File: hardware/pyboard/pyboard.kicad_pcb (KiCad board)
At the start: 2 copper layers, 65 parts, among them J1 Battery, J2 Arduino_Mega2560_Shield, J6 USB_B_Micro, J9 Micro_SD_SCHA5B0200, Q1 IRLML6402, Q2 IRLML6402, SW1 RST, SW2 USR, U1 STM32F405RGT6, U2 MCP1703A-3302_SOT89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

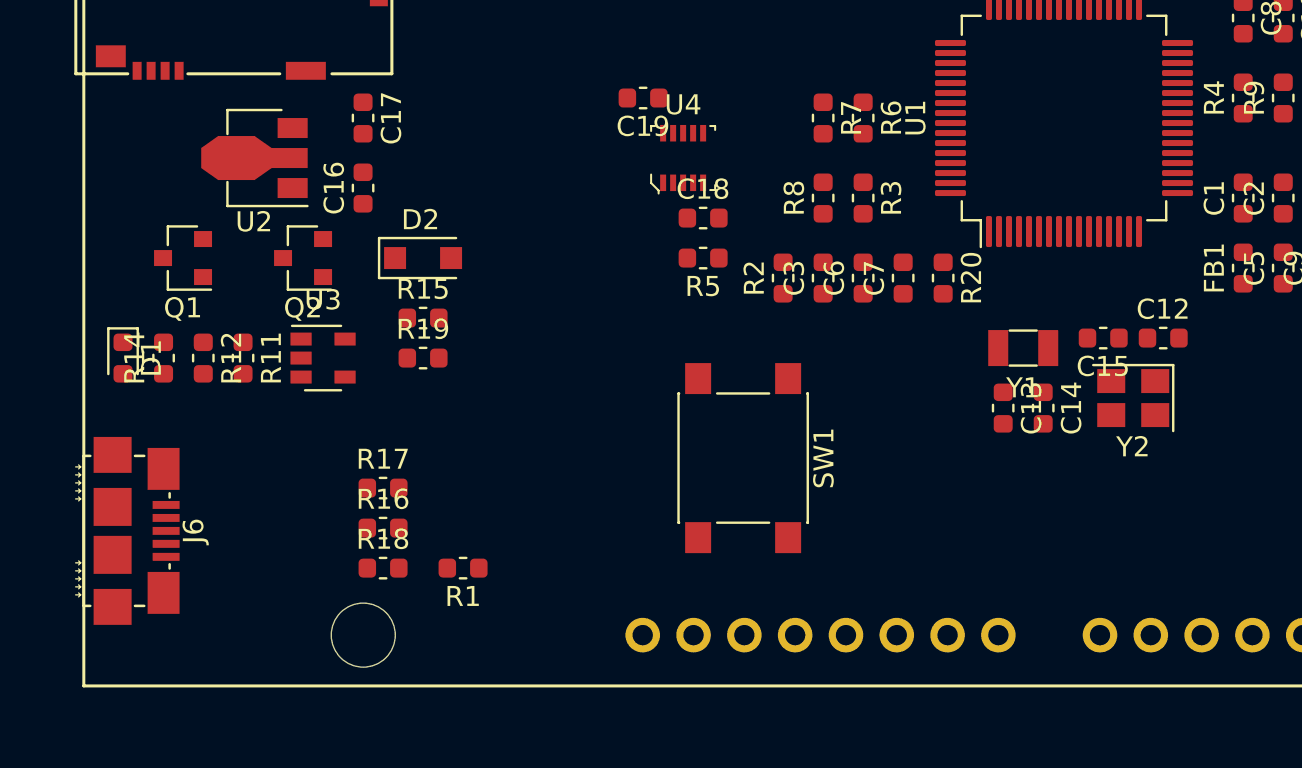
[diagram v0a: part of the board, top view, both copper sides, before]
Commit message: Route crystal oscillator
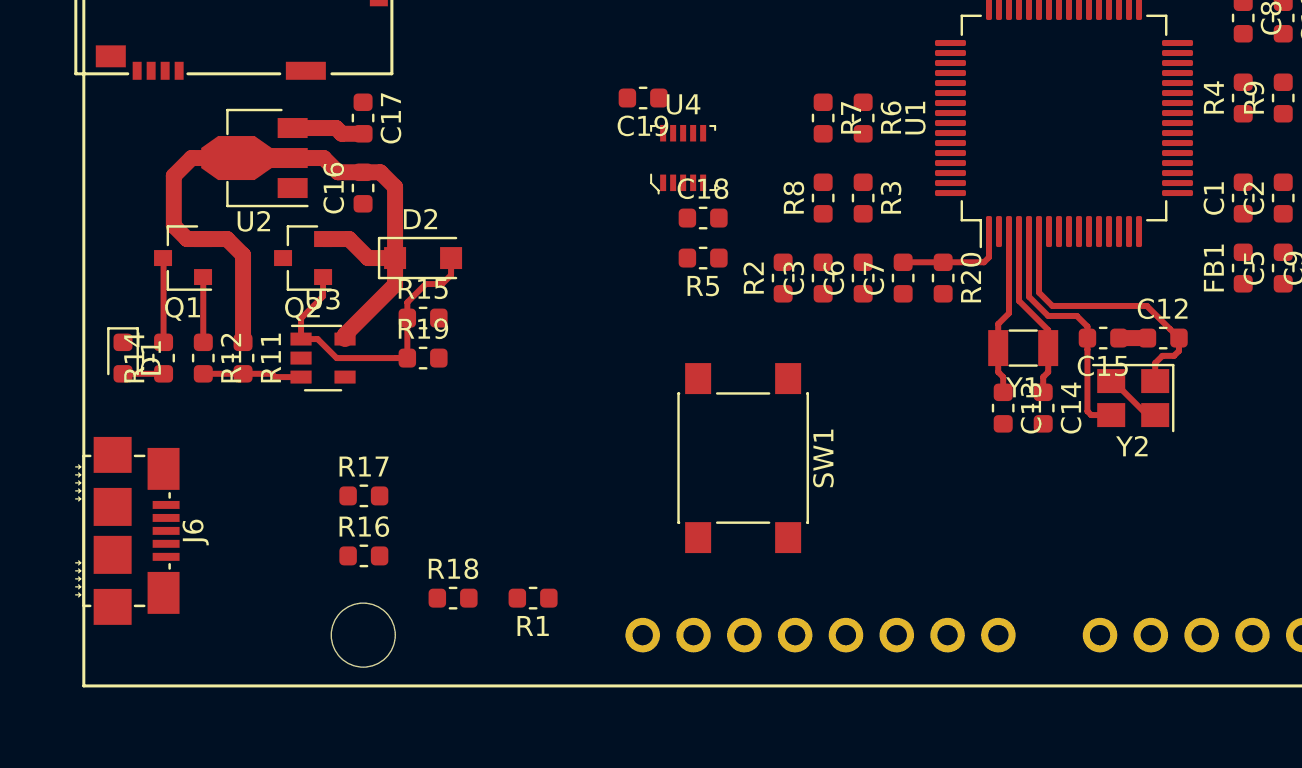
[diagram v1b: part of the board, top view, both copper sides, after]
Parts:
- moved R1 3.81 mm to (122.5, 115.6)
- moved R18 3.81 mm to (118.5, 115.6)
- moved R16 1.69 mm to (114.0, 113.5)
- moved R17 1.04 mm to (114.0, 110.5)
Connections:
- net /DM_USB renamed /USB_D-
- net /DP_USB renamed /USB_D+
- D2 pad 2: /VBUS_USB -> /USB_VBUS
- J6 pad GND: GND -> (no net)
- J6 pad ID: /ID_USB -> (no net)
- J6 pad VBUS: /VBUS_USB -> (no net)
- Q2 pad 1: /VBUS_USB -> /USB_VBUS
- R15 pad 1: /VBUS_USB -> /USB_VBUS
- R18 pad 1: /ID_USB -> (no net)
- R19 pad 1: /VBUS_USB -> /USB_VBUS
- U3 pad 1: /VBUS_USB -> /USB_VBUS
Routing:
- net VCC: track 0.00 -> 31.6 mm
- net /USB_VBUS: track 0.00 -> 15.6 mm
- net Net-(C12-Pad2): track 0.10 -> 14.1 mm
- net Net-(C15-Pad2): track 0.00 -> 12.3 mm
- net /N2: track 0.00 -> 9.15 mm
- net /N1: track 0.00 -> 8.36 mm
- net /VRTC: track 0.00 -> 5.68 mm
- net /~OC: track 0.00 -> 4.95 mm
- net GND: track 0.00 -> 4.33 mm
- net Net-(Q1-Pad3): track 0.00 -> 4.22 mm
- net +3V3: track 0.00 -> 3.64 mm
- net Net-(Q1-Pad1): track 0.00 -> 3.27 mm
- net Net-(D1-Pad2): track 0.00 -> 2.03 mm

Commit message: Trace USB
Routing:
- net /USB_D+: track 0.00 -> 10.7 mm
- net /USB_D-: track 0.00 -> 9.55 mm
- net +3V3: track 3.64 -> 9.12 mm
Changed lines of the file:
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@@
     (thickness 1.6)
     (drawings 0)
-    (tracks 88)
+    (tracks 102)
     (zones 0)
     (modules 65)
@@
     (uvia_dia 0.3)
     (uvia_drill 0.1)
+    (add_net +3V3)
     (add_net /B)
     (add_net /BLU)
@@
     (add_net "Net-(J1-Pad1)")
     (add_net "Net-(J2-Pad5V4)")
-    (add_net "Net-(J2-PadA14)")
-    (add_net "Net-(J2-PadA15)")
-    (add_net "Net-(J2-PadAREF)")
-    (add_net "Net-(J2-PadD16)")
-    (add_net "Net-(J2-PadD17)")
-    (add_net "Net-(J2-PadD18)")
-    (add_net "Net-(J2-PadD19)")
-    (add_net "Net-(J2-PadD22)")
-    (add_net "Net-(J2-PadD23)")
-    (add_net "Net-(J2-PadD24)")
-    (add_net "Net-(J2-PadD25)")
-    (add_net "Net-(J2-PadD26)")
-    (add_net "Net-(J2-PadD27)")
-    (add_net "Net-(J2-PadD28)")
-    (add_net "Net-(J2-PadD29)")
-    (add_net "Net-(J2-PadD30)")
-    (add_net "Net-(J2-PadD31)")
-    (add_net "Net-(J2-PadD32)")
-    (add_net "Net-(J2-PadD33)")
-    (add_net "Net-(J2-PadD34)")
-    (add_net "Net-(J2-PadD35)")
-    (add_net "Net-(J2-PadD36)")
-    (add_net "Net-(J2-PadD37)")
-    (add_net "Net-(J2-PadD38)")
-    (add_net "Net-(J2-PadD39)")
-    (add_net "Net-(J2-PadD40)")
-    (add_net "Net-(J2-PadD41)")
-    (add_net "Net-(J2-PadD42)")
-    (add_net "Net-(J2-PadD43)")
-    (add_net "Net-(J2-PadD44)")
-    (add_net "Net-(J2-PadD45)")
-    (add_net "Net-(J2-PadD46)")
-    (add_net "Net-(J2-PadD47)")
-    (add_net "Net-(J2-PadD48)")
-    (add_net "Net-(J2-PadD49)")
-    (add_net "Net-(J2-PadD50)")
-    (add_net "Net-(J2-PadD51)")
-    (add_net "Net-(J2-PadD52)")
-    (add_net "Net-(J2-PadD53)")
-    (add_net "Net-(J2-PadIORF)")
     (add_net "Net-(Q1-Pad1)")
     (add_net "Net-(Q1-Pad3)")
@@
     (uvia_dia 0.3)
     (uvia_drill 0.1)
-    (add_net +3V3)
     (add_net GND)
     (add_net VCC)
@@
   (segment (start 153.16 106.46) (end 151.46 104.76) (width 0.3) (layer F.Cu) (net 1))
   (segment (start 153.56 106.46) (end 153.16 106.46) (width 0.3) (layer F.Cu) (net 1))
-  (segment (start 113.96 92.3975) (end 112.8975 92.3975) (width 0.8) (layer F.Cu) (net 2))
-  (segment (start 112.61 92.11) (end 110.44 92.11) (width 0.8) (layer F.Cu) (net 2))
-  (segment (start 112.8975 92.3975) (end 112.61 92.11) (width 0.8) (layer F.Cu) (net 2))
+  (segment (start 110.44 92.11) (end 112.61 92.11) (width 0.3) (layer F.Cu) (net 2))
+  (segment (start 112.8975 92.3975) (end 113.96 92.3975) (width 0.3) (layer F.Cu) (net 2))
+  (segment (start 112.61 92.11) (end 112.8975 92.3975) (width 0.3) (layer F.Cu) (net 2))
+  (segment (start 154.675 94.36) (end 156.36 94.36) (width 0.3) (layer F.Cu) (net 2))
+  (segment (start 159.96 94.8225) (end 156.8225 94.8225) (width 0.3) (layer F.Cu) (net 2))
+  (segment (start 156.8225 94.8225) (end 156.36 94.36) (width 0.3) (layer F.Cu) (net 2))
   (segment (start 145.25 97.285) (end 145.25 98.5725) (width 0.3) (layer F.Cu) (net 5))
   (segment (start 145 98.8225) (end 142.96 98.8225) (width 0.3) (layer F.Cu) (net 5))
@@
   (segment (start 148.21 102.21) (end 146.75 100.75) (width 0.3) (layer F.Cu) (net 10))
   (segment (start 148.21 103.11) (end 148.21 102.21) (width 0.3) (layer F.Cu) (net 10))
+  (segment (start 104.262929 112.101531) (end 105.028991 112.101531) (width 0.2) (layer F.Cu) (net 73))
+  (segment (start 104.11462 112.24984) (end 104.262929 112.101531) (width 0.2) (layer F.Cu) (net 73))
+  (segment (start 105.028991 112.101531) (end 106.180522 110.95) (width 0.2) (layer F.Cu) (net 73))
+  (segment (start 106.180522 110.95) (end 110.6625 110.95) (width 0.2) (layer F.Cu) (net 73))
+  (segment (start 110.6625 110.95) (end 113.2125 113.5) (width 0.2) (layer F.Cu) (net 73))
+  (segment (start 105.980282 110.5) (end 110.6625 110.5) (width 0.2) (layer F.Cu) (net 74))
+  (segment (start 110.6625 110.5) (end 113.2125 110.5) (width 0.2) (layer F.Cu) (net 74))
+  (segment (start 105.028991 111.451291) (end 105.980282 110.5) (width 0.2) (layer F.Cu) (net 74))
+  (segment (start 104.11462 111.60214) (end 104.125923 111.60214) (width 0.2) (layer F.Cu) (net 74))
+  (segment (start 104.125923 111.60214) (end 104.276772 111.451291) (width 0.2) (layer F.Cu) (net 74))
+  (segment (start 104.276772 111.451291) (end 105.028991 111.451291) (width 0.2) (layer F.Cu) (net 74))
 )

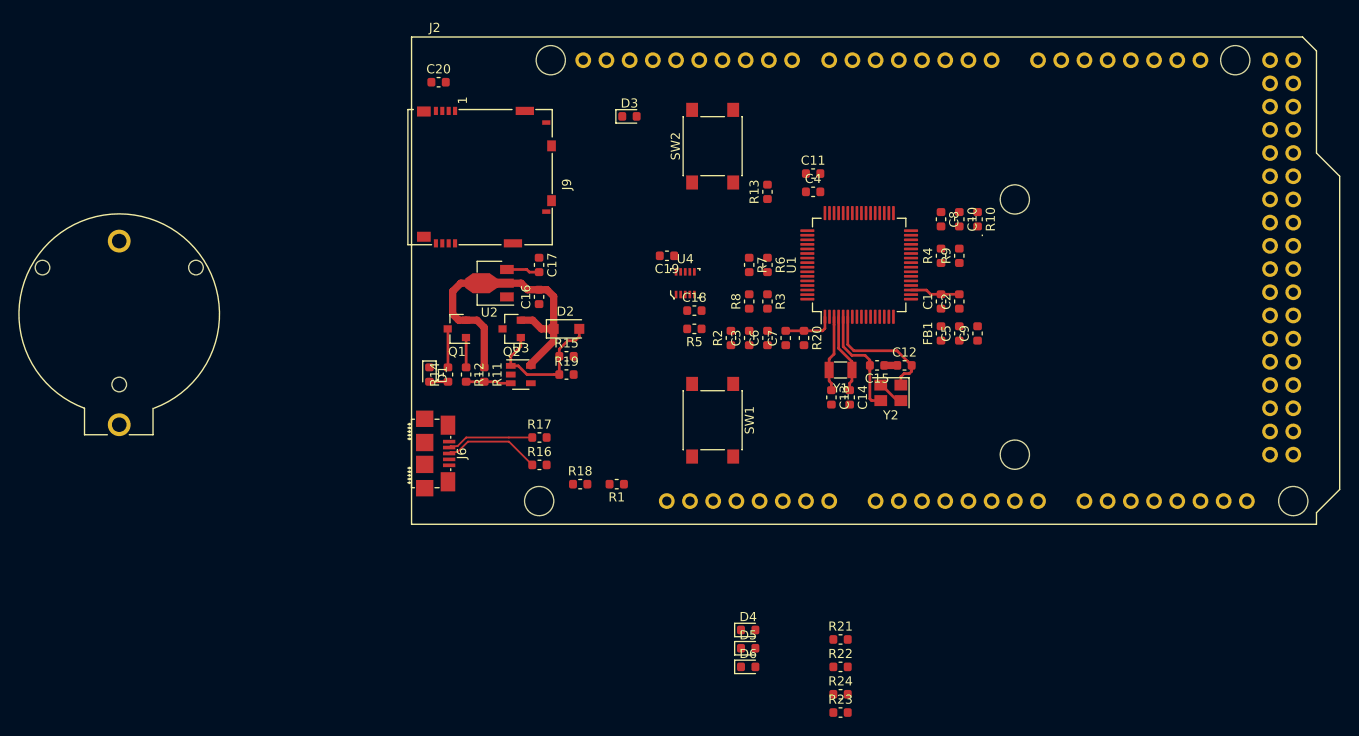
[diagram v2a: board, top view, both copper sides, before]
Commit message: Trace SDIO #1
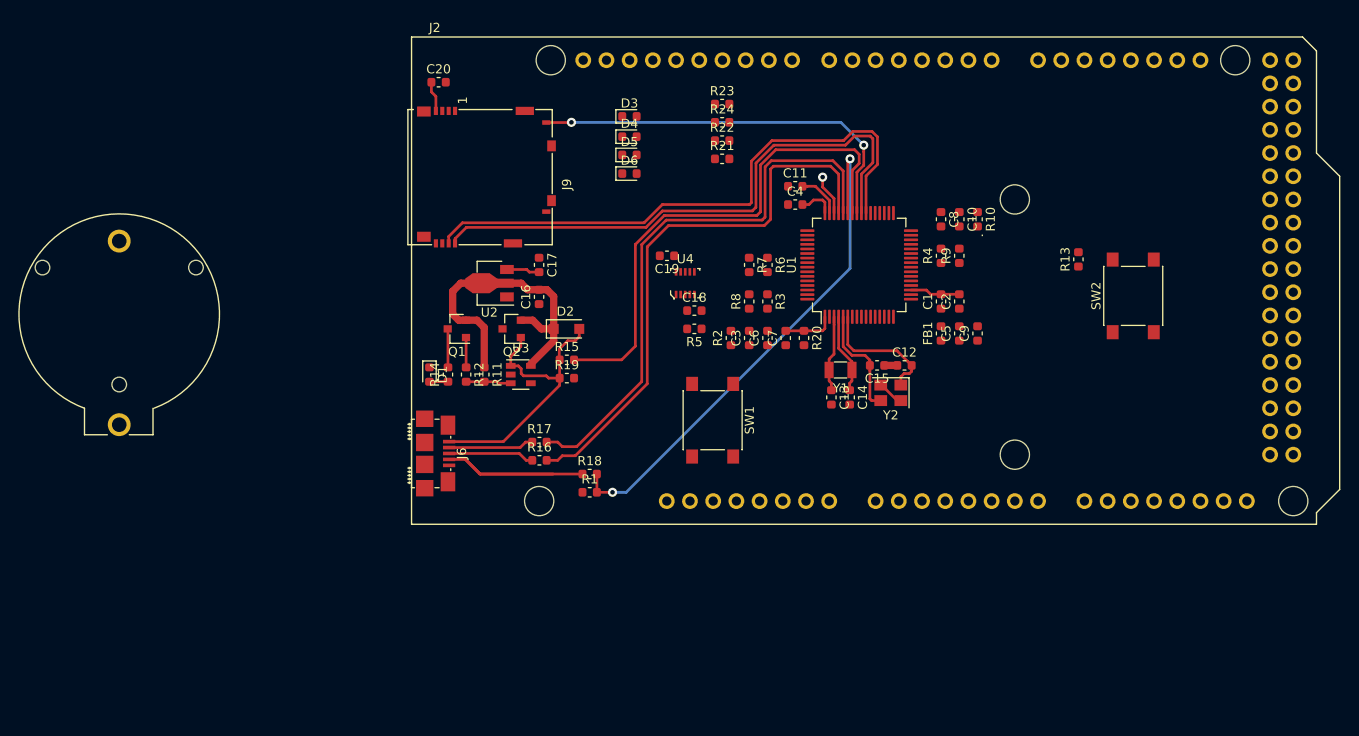
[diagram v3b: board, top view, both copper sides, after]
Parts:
- moved R23 67.9 mm to (134.0, 74.0)
- moved R24 63.9 mm to (134.0, 76.0)
- moved R22 59.0 mm to (134.0, 78.0)
- moved D6 55.5 mm to (123.9, 81.6)
- moved D4 55.5 mm to (123.9, 77.6)
- moved D5 55.5 mm to (123.9, 79.6)
- moved R21 54.2 mm to (134.0, 80.0)
- moved SW2 48.9 mm to (179.0, 95.0)
- moved R13 34.8 mm to (173.0, 91.0)
- moved R1 3.09 mm to (119.5, 116.5), turned to 0 degrees
- moved C11 2.40 mm to (142.0, 83.0)
- moved C4 2.40 mm to (142.0, 85.0)
- moved R18 1.52 mm to (119.5, 114.5)
- moved R16 0.50 mm to (114.0, 113.0)
- moved R17 0.50 mm to (114.0, 111.0)
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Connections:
- net /DM renamed /D-
- net /DP renamed /D+
- J6 pad GND: (no net) -> GND
- J6 pad ID: (no net) -> /USB_ID
- J6 pad VBUS: (no net) -> /USB_VBUS
- R18 pad 1: (no net) -> /USB_ID
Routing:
- net /SDIO_D0: track 0.00 -> 64.2 mm
- net /D-: track 0.00 -> 62.7 mm
- net /SDIO_D1: track 0.00 -> 62.5 mm
- net /D+: track 0.00 -> 61.9 mm
- net /ID: track 0.00 -> 57.9 mm, vias 0 -> 2
- net /VBUS: track 0.00 -> 57.2 mm
- net /SDIO_SW: track 0.00 -> 43.5 mm, vias 0 -> 2
- net /USB_ID: track 0.00 -> 25.5 mm
- net /USB_VBUS: track 15.6 -> 31.6 mm
- net +3V3: track 9.12 -> 16.4 mm
- net /VCAP_2: track 0.00 -> 4.99 mm
- net /RED: track 0.00 -> 4.45 mm, vias 0 -> 1
- net /USB_D+: track 10.7 -> 9.41 mm
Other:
- net class Default: via_dia 0.8 -> 1; via_drill 0.4 -> 0.5
- net class Power: via_dia 0.8 -> 1; via_drill 0.4 -> 0.5

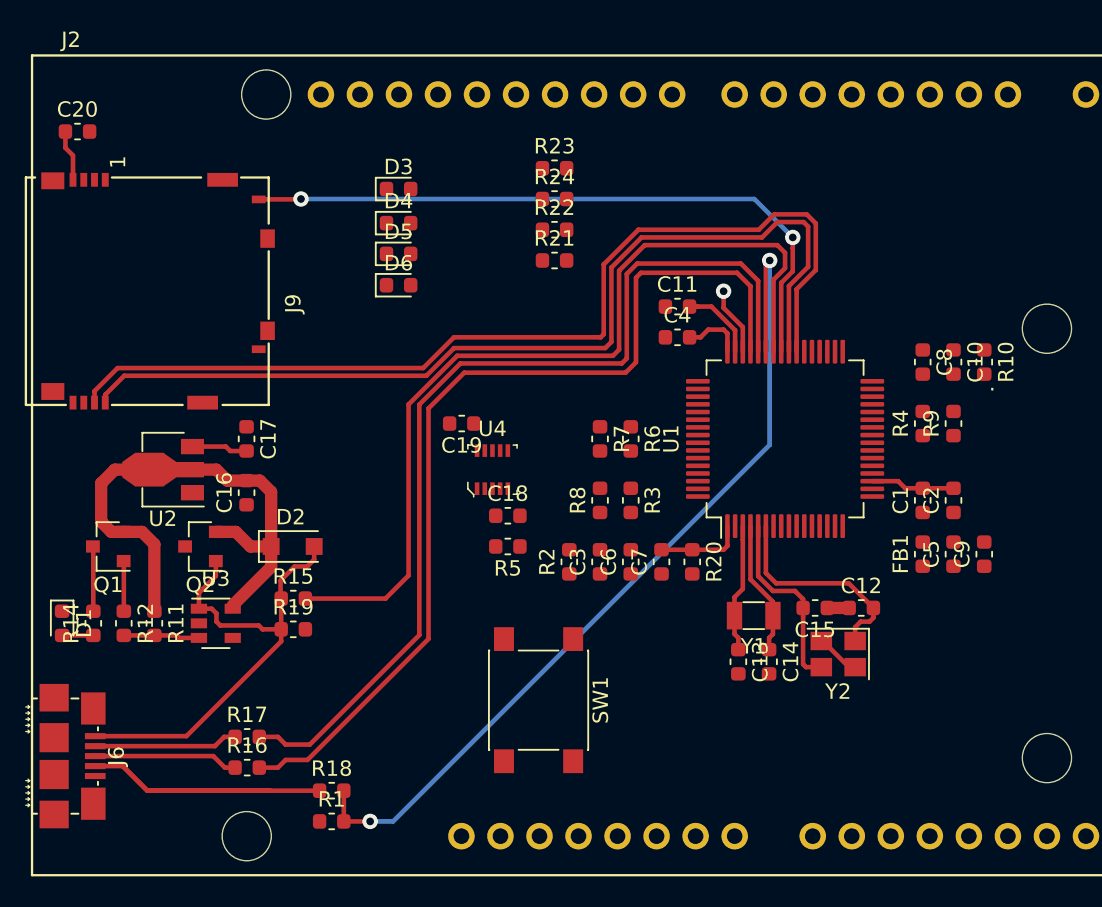
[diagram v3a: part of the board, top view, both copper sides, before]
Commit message: Fix USB terminal resistors
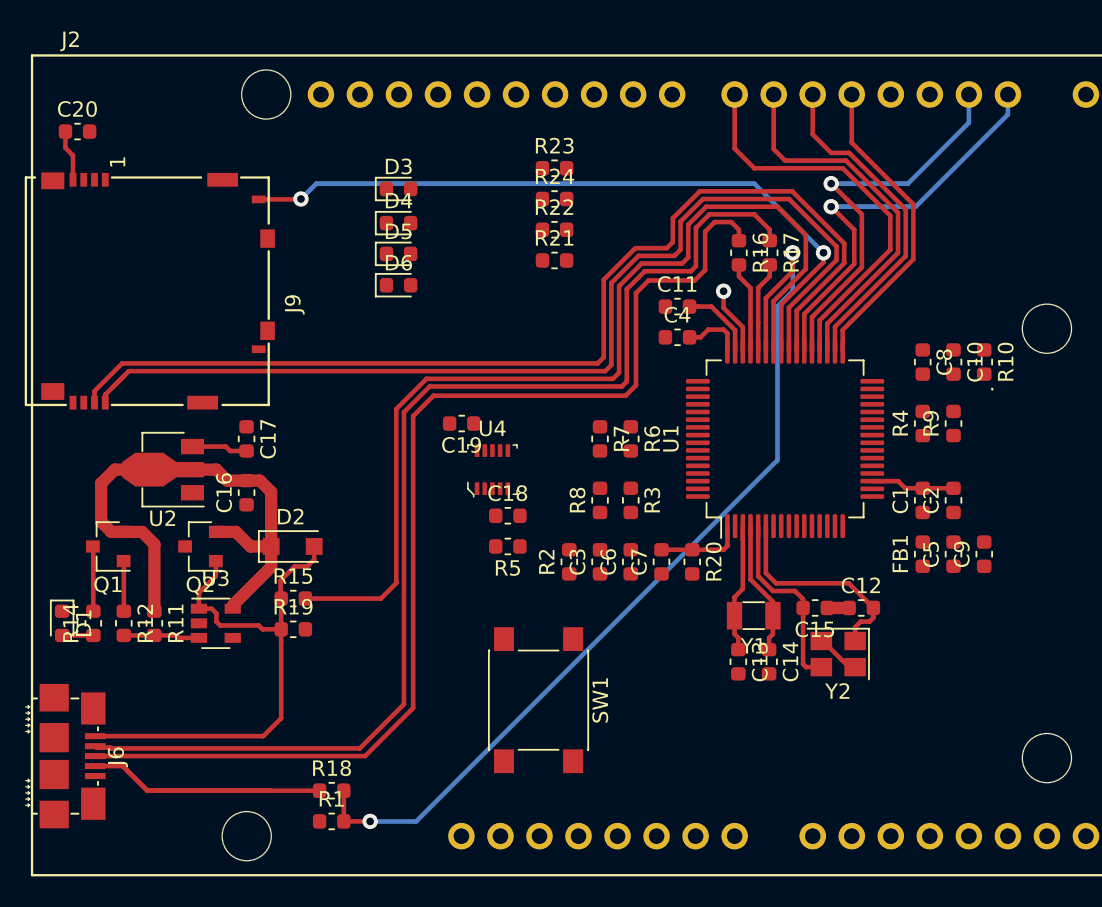
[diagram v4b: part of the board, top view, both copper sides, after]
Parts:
- moved R17 46.3 mm to (148.0, 79.5), turned to 270 degrees
- moved R16 46.3 mm to (146.0, 79.5), turned to 270 degrees
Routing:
- net /USB_D-: track 9.35 -> 75.6 mm
- net /USB_D+: track 9.41 -> 73.3 mm
- net /D-: track 62.7 -> 5.96 mm
- net /D+: track 61.9 -> 5.96 mm
- net /Y2: track 0.00 -> 26.7 mm, vias 0 -> 1
- net /Y1: track 0.00 -> 26.3 mm, vias 0 -> 1
- net /Y8: track 0.00 -> 26.2 mm
- net /Y7: track 0.00 -> 24.3 mm
- net /Y6: track 0.00 -> 22.1 mm
- net /Y5: track 0.00 -> 20.3 mm
- net /VBUS: track 57.2 -> 63.5 mm
- net /SDIO_D1: track 62.5 -> 68.0 mm
- net /SDIO_D0: track 64.2 -> 68.5 mm
- net /ID: track 57.9 -> 61.0 mm
- net /SDIO_SW: track 43.5 -> 46.6 mm
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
